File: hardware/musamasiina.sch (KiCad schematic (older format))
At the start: 59 parts, among them P1 USB_OTG, P2 SJ1-352XN, P3 SJ1-352XN, P4 SJ1-352XN, SW1 SW_PUSH, U2 WT32, U4 LTC6257

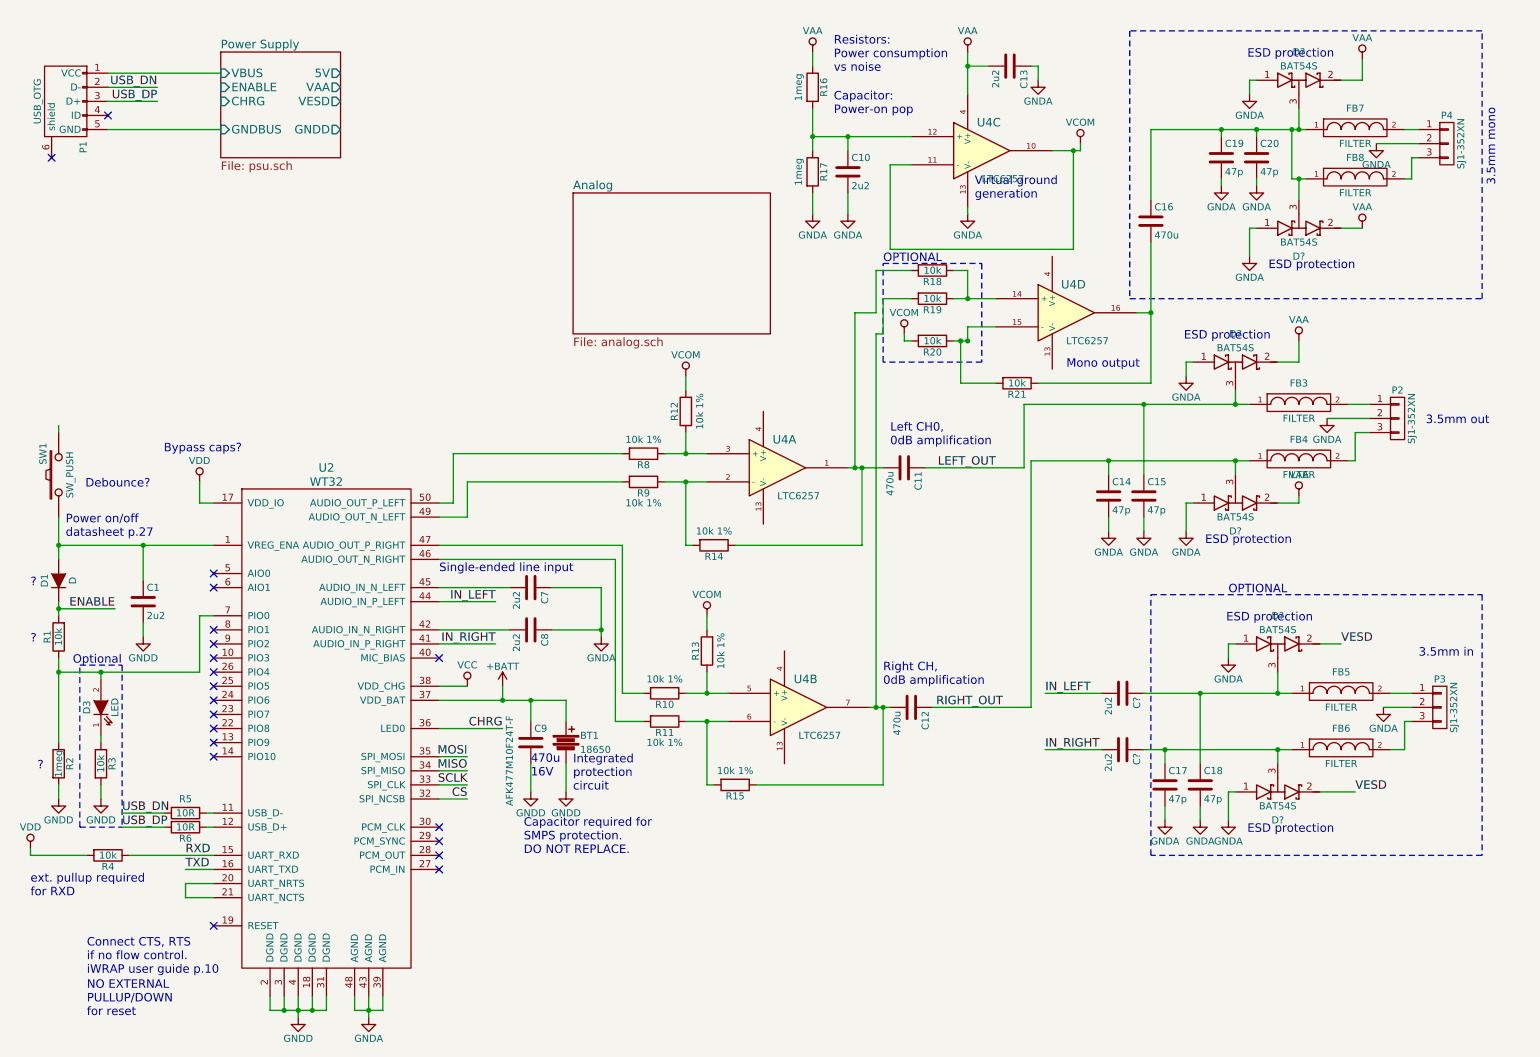
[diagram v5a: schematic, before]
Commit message: Add user IO, programming headers
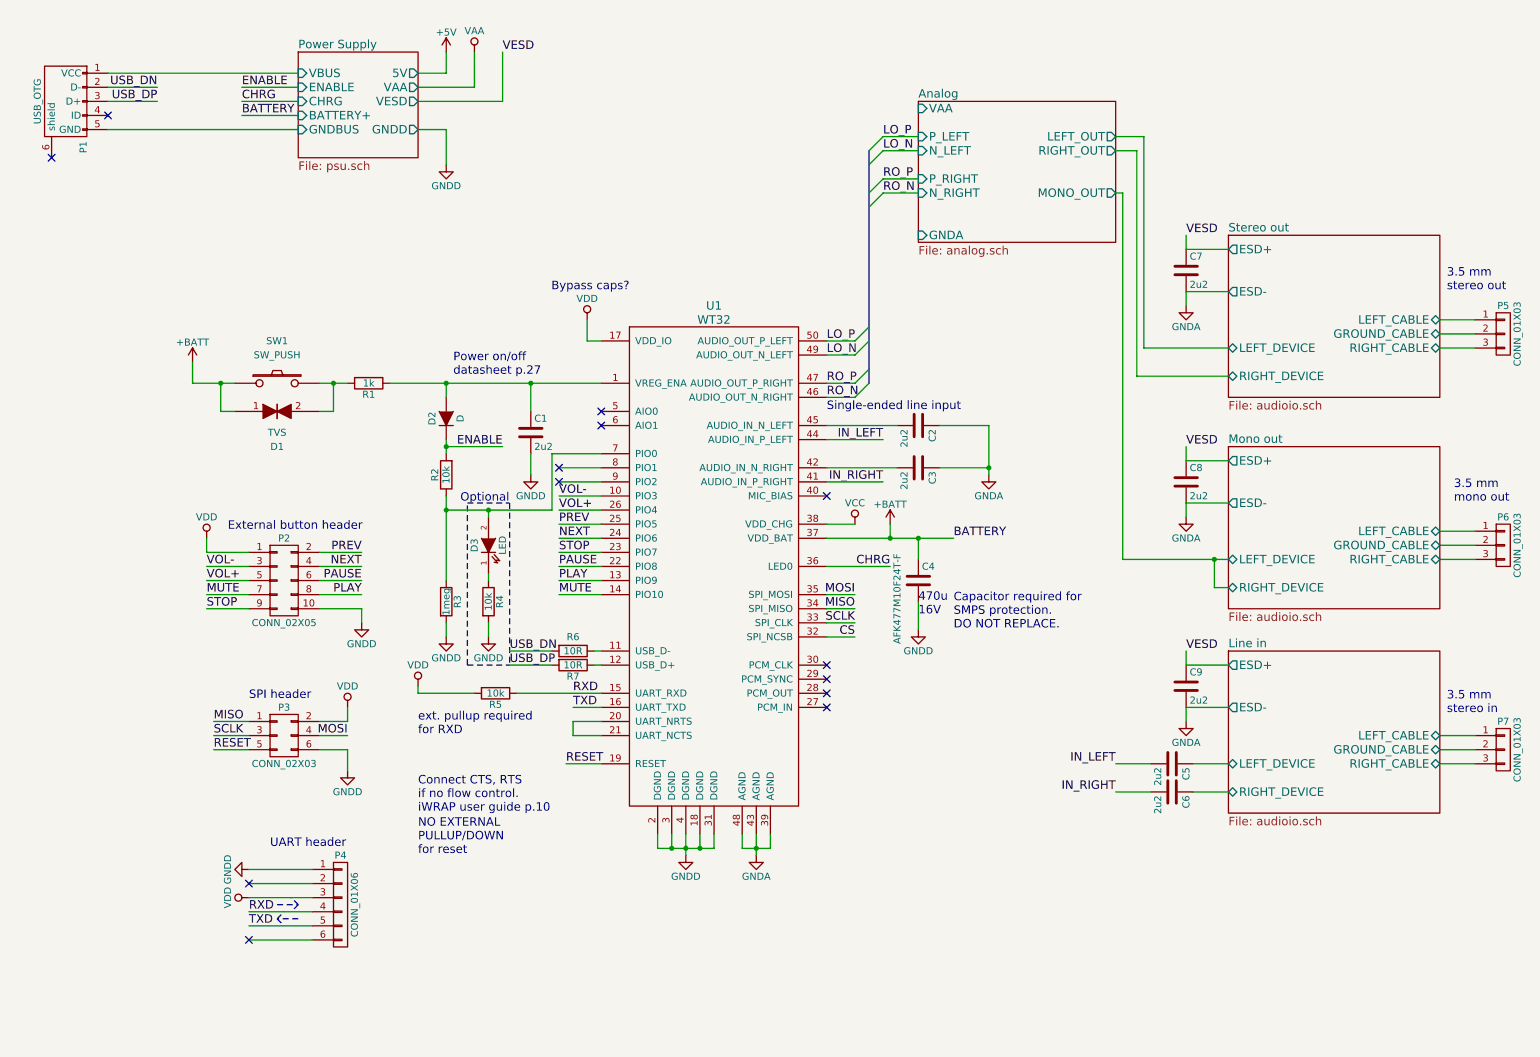
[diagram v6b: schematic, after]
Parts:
- removed BT1: 18650, symbol Battery
- removed C10, C13, C? (x2): 2u2, symbol C
- removed C11, C12, C16: 470u, symbol C
- removed C14, C15, C17, C18, C19, C20: 47p, symbol C
- removed D? (x6): BAT54S, symbol BAT54S
- removed FB3, FB4, FB5, FB6, FB7, FB8: FILTER, symbol FILTER
- removed P2, P3, P4: SJ1-352XN, symbol CONN_01X03
- removed R10, R11, R12, R13, R14, R15, R8, R9: 10k 1%, symbol R
- removed R16, R17: 1meg, symbol R
- removed R18, R19, R20, R21: 10k, symbol R
- removed U4: LTC6257, symbol LTC6242
- added C5, C6, C7, C8, C9: 2u2, symbol C
- added D1: TVS, symbol TVS
- added P2: CONN_02X05, symbol CONN_02X05
- added P3: CONN_02X03, symbol CONN_02X03
- added P4: CONN_01X06, symbol CONN_01X06
- added P5, P6, P7: CONN_01X03, symbol CONN_01X03
- added R1: 1k, symbol R
- renumbered C7 to C2, C8 to C3, C9 to C4, D1 to D2, R1 to R2, R2 to R3, R3 to R4, R4 to R5, R5 to R6, R6 to R7, U2 to U1
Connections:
- net +BATT: now also SW1.1, D1.1
- net GNDA: now also C7.2, C8.2, C9.2
- net GNDD: now also P2.10 (P10), P3.6 (P6), P4.1 (P1)
- net IN_LEFT: now also C5.2
- net IN_RIGHT: now also C6.2
- net MISO: now also P3.1 (P1)
- net MOSI: now also P3.4 (P4)
- net RXD: now also P4.4 (P4)
- net SCLK: now also P3.3 (P3)
- net TXD: now also P4.5 (P5)
- net VDD: now also P2.1 (P1), P3.2 (P2), P4.3 (P3)
- net VESD: now also C7.1, C8.1, C9.1
- net at C1.1, D2.2 (A), U1.1 (VREG_ENA): now also R1.1; no longer SW1.1
- net VOL-: now reaches U1.10 (PIO3)
- net VOL-: now also P2.3 (P3)
- net PLAY: now reaches U1.13 (PIO9)
- net PLAY: now also P2.8 (P8)
- net MUTE: now reaches U1.14 (PIO10)
- net MUTE: now also P2.7 (P7)
- net RESET: now reaches U1.19 (RESET)
- net RESET: now also P3.5 (P5)
- net PAUSE: now reaches U1.22 (PIO8)
- net PAUSE: now also P2.6 (P6)
- net STOP: now reaches U1.23 (PIO7)
- net STOP: now also P2.9 (P9)
- net NEXT: now reaches U1.24 (PIO6)
- net NEXT: now also P2.4 (P4)
- net PREV: now reaches U1.25 (PIO5)
- net PREV: now also P2.2 (P2)
- net VOL+: now reaches U1.26 (PIO4)
- net VOL+: now also P2.5 (P5)
- net RO_N: now reaches U1.46 (AUDIO_OUT_N_RIGHT)
- net RO_P: now reaches U1.47 (AUDIO_OUT_P_RIGHT)
- net LO_N: now reaches U1.49 (AUDIO_OUT_N_LEFT)
- net LO_P: now reaches U1.50 (AUDIO_OUT_P_LEFT)
- net at SW1.2: now also D1.2, R1.2
- new net Line in/GROUND_CABLE: P7.2 (P2)
- new net Line in/LEFT_CABLE: P7.1 (P1)
- new net Line in/LEFT_DEVICE: C5.1
- new net Line in/RIGHT_CABLE: P7.3 (P3)
- new net Line in/RIGHT_DEVICE: C6.1
- new net Mono out/GROUND_CABLE: P6.2 (P2)
- new net Mono out/LEFT_CABLE: P6.1 (P1)
- new net Mono out/RIGHT_CABLE: P6.3 (P3)
- new net Stereo out/GROUND_CABLE: P5.2 (P2)
- new net Stereo out/LEFT_CABLE: P5.1 (P1)
- new net Stereo out/RIGHT_CABLE: P5.3 (P3)
- no-connect marks 20 -> 13
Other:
- note added: "3.5 mm\nmono out"
- note added: "3.5 mm\nstereo in"
- note added: "3.5 mm\nstereo out"
- note added: "External button header"
- note added: "SPI header"
- note added: "UART header"
- note removed: "3.5mm in"
- note removed: "3.5mm mono"
- note removed: "3.5mm out"
- note removed: "?"
- note removed: "Capacitor: \nPower-on pop"
- note removed: "Debounce?"
- note removed: "ESD protection"
- note removed: "Integrated \nprotection\ncircuit"
- note removed: "Left CH0,\n0dB amplification"
- note removed: "Mono output"
- note removed: "OPTIONAL"
- note removed: "Resistors:\nPower consumption\nvs noise"
- note removed: "Right CH,\n0dB amplification"
- note removed: "Virtual ground\ngeneration"
- moved on the sheet: C1, C2, C3, C4, D2, D3, R2, R3, R4, R5, R6, R7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
